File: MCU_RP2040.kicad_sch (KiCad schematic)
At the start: 34 parts, among them X1 ECS-2520MVLC-120-CN

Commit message: Annotation update
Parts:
- renumbered C13 to C7, C15 to C8
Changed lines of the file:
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@@
 			(project "Mad_RP2040"
 				(path "/eedae293-eb5b-47bd-b383-bccfdf81bf72/4e3cb99d-3a42-46ca-abb7-444fcb451820/f42afd4d-da97-4905-9d8b-11c28a037c21"
-					(reference "TP?")
+					(reference "TP2")
 					(unit 1)
 				)
@@
 			(project "Mad_RP2040"
 				(path "/eedae293-eb5b-47bd-b383-bccfdf81bf72/4e3cb99d-3a42-46ca-abb7-444fcb451820/f42afd4d-da97-4905-9d8b-11c28a037c21"
-					(reference "C?")
+					(reference "C14")
 					(unit 1)
 				)
@@
 			(project "Mad_RP2040"
 				(path "/eedae293-eb5b-47bd-b383-bccfdf81bf72/4e3cb99d-3a42-46ca-abb7-444fcb451820/f42afd4d-da97-4905-9d8b-11c28a037c21"
-					(reference "Q?")
+					(reference "Q1")
 					(unit 2)
 				)
@@
 			(project "Mad_RP2040"
 				(path "/eedae293-eb5b-47bd-b383-bccfdf81bf72/4e3cb99d-3a42-46ca-abb7-444fcb451820/f42afd4d-da97-4905-9d8b-11c28a037c21"
-					(reference "R?")
+					(reference "R7")
 					(unit 1)
 				)
@@
 			(project "Mad_RP2040"
 				(path "/eedae293-eb5b-47bd-b383-bccfdf81bf72/4e3cb99d-3a42-46ca-abb7-444fcb451820/f42afd4d-da97-4905-9d8b-11c28a037c21"
-					(reference "U?")
+					(reference "U5")
 					(unit 1)
 				)
@@
 			(project "Mad_RP2040"
 				(path "/eedae293-eb5b-47bd-b383-bccfdf81bf72/4e3cb99d-3a42-46ca-abb7-444fcb451820/f42afd4d-da97-4905-9d8b-11c28a037c21"
-					(reference "R?")
+					(reference "R6")
 					(unit 1)
 				)
@@
 			(project "Mad_RP2040"
 				(path "/eedae293-eb5b-47bd-b383-bccfdf81bf72/4e3cb99d-3a42-46ca-abb7-444fcb451820/f42afd4d-da97-4905-9d8b-11c28a037c21"
-					(reference "C?")
+					(reference "C9")
 					(unit 1)
 				)
@@
 			(project "Mad_RP2040"
 				(path "/eedae293-eb5b-47bd-b383-bccfdf81bf72/4e3cb99d-3a42-46ca-abb7-444fcb451820/f42afd4d-da97-4905-9d8b-11c28a037c21"
-					(reference "C?")
+					(reference "C10")
 					(unit 1)
 				)
@@
 			(project "Mad_RP2040"
 				(path "/eedae293-eb5b-47bd-b383-bccfdf81bf72/4e3cb99d-3a42-46ca-abb7-444fcb451820/f42afd4d-da97-4905-9d8b-11c28a037c21"
-					(reference "C?")
+					(reference "C13")
 					(unit 1)
 				)
@@
 			(project "Mad_RP2040"
 				(path "/eedae293-eb5b-47bd-b383-bccfdf81bf72/4e3cb99d-3a42-46ca-abb7-444fcb451820/f42afd4d-da97-4905-9d8b-11c28a037c21"
-					(reference "C?")
+					(reference "C11")
 					(unit 1)
 				)
@@
 			(project "Mad_RP2040"
 				(path "/eedae293-eb5b-47bd-b383-bccfdf81bf72/4e3cb99d-3a42-46ca-abb7-444fcb451820/f42afd4d-da97-4905-9d8b-11c28a037c21"
-					(reference "U?")
+					(reference "U4")
 					(unit 1)
 				)
@@
 			(project "Mad_RP2040"
 				(path "/eedae293-eb5b-47bd-b383-bccfdf81bf72/4e3cb99d-3a42-46ca-abb7-444fcb451820/f42afd4d-da97-4905-9d8b-11c28a037c21"
-					(reference "TP?")
+					(reference "TP3")
 					(unit 1)
 				)
@@
 			(project "Mad_RP2040"
 				(path "/eedae293-eb5b-47bd-b383-bccfdf81bf72/4e3cb99d-3a42-46ca-abb7-444fcb451820/f42afd4d-da97-4905-9d8b-11c28a037c21"
-					(reference "C?")
+					(reference "C6")
 					(unit 1)
 				)
@@
 			(project "Mad_RP2040"
 				(path "/eedae293-eb5b-47bd-b383-bccfdf81bf72/4e3cb99d-3a42-46ca-abb7-444fcb451820/f42afd4d-da97-4905-9d8b-11c28a037c21"
-					(reference "D?")
+					(reference "D7")
 					(unit 1)
 				)
@@
 			(project "Mad_RP2040"
 				(path "/eedae293-eb5b-47bd-b383-bccfdf81bf72/4e3cb99d-3a42-46ca-abb7-444fcb451820/f42afd4d-da97-4905-9d8b-11c28a037c21"
-					(reference "C?")
+					(reference "C16")
 					(unit 1)
 				)
@@
 			(project "Mad_RP2040"
 				(path "/eedae293-eb5b-47bd-b383-bccfdf81bf72/4e3cb99d-3a42-46ca-abb7-444fcb451820/f42afd4d-da97-4905-9d8b-11c28a037c21"
-					(reference "Q?")
+					(reference "Q1")
 					(unit 1)
 				)
@@
 			(project "Mad_RP2040"
 				(path "/eedae293-eb5b-47bd-b383-bccfdf81bf72/4e3cb99d-3a42-46ca-abb7-444fcb451820/f42afd4d-da97-4905-9d8b-11c28a037c21"
-					(reference "R?")
+					(reference "R9")
 					(unit 1)
 				)
@@
 		(on_board yes)
 		(dnp no)
-		(property "Reference" "C13"
+		(property "Reference" "C7"
 			(at 52.705 73.66 0)
 			(effects
@@
 			(project "Mad_RP2040"
 				(path "/eedae293-eb5b-47bd-b383-bccfdf81bf72/4e3cb99d-3a42-46ca-abb7-444fcb451820/f42afd4d-da97-4905-9d8b-11c28a037c21"
-					(reference "C13")
+					(reference "C7")
 					(unit 1)
 				)
@@
 			(project "Mad_RP2040"
 				(path "/eedae293-eb5b-47bd-b383-bccfdf81bf72/4e3cb99d-3a42-46ca-abb7-444fcb451820/f42afd4d-da97-4905-9d8b-11c28a037c21"
-					(reference "C?")
+					(reference "C17")
 					(unit 1)
 				)
@@
 			(project "Mad_RP2040"
 				(path "/eedae293-eb5b-47bd-b383-bccfdf81bf72/4e3cb99d-3a42-46ca-abb7-444fcb451820/f42afd4d-da97-4905-9d8b-11c28a037c21"
-					(reference "C?")
+					(reference "C12")
 					(unit 1)
 				)
@@
 			(project "Mad_RP2040"
 				(path "/eedae293-eb5b-47bd-b383-bccfdf81bf72/4e3cb99d-3a42-46ca-abb7-444fcb451820/f42afd4d-da97-4905-9d8b-11c28a037c21"
-					(reference "C?")
+					(reference "C15")
 					(unit 1)
 				)
@@
 			(project "Mad_RP2040"
 				(path "/eedae293-eb5b-47bd-b383-bccfdf81bf72/4e3cb99d-3a42-46ca-abb7-444fcb451820/f42afd4d-da97-4905-9d8b-11c28a037c21"
-					(reference "TP?")
+					(reference "TP1")
 					(unit 1)
 				)
@@
 			(project "Mad_RP2040"
 				(path "/eedae293-eb5b-47bd-b383-bccfdf81bf72/4e3cb99d-3a42-46ca-abb7-444fcb451820/f42afd4d-da97-4905-9d8b-11c28a037c21"
-					(reference "R?")
+					(reference "R12")
 					(unit 1)
 				)
@@
 			(project "Mad_RP2040"
 				(path "/eedae293-eb5b-47bd-b383-bccfdf81bf72/4e3cb99d-3a42-46ca-abb7-444fcb451820/f42afd4d-da97-4905-9d8b-11c28a037c21"
-					(reference "R?")
+					(reference "R8")
 					(unit 1)
 				)
@@
 			(project "Mad_RP2040"
 				(path "/eedae293-eb5b-47bd-b383-bccfdf81bf72/4e3cb99d-3a42-46ca-abb7-444fcb451820/f42afd4d-da97-4905-9d8b-11c28a037c21"
-					(reference "R?")
+					(reference "R13")
 					(unit 1)
 				)
@@
 			(project "Mad_RP2040"
 				(path "/eedae293-eb5b-47bd-b383-bccfdf81bf72/4e3cb99d-3a42-46ca-abb7-444fcb451820/f42afd4d-da97-4905-9d8b-11c28a037c21"
-					(reference "R?")
+					(reference "R14")
 					(unit 1)
 				)
@@
 			(project "Mad_RP2040"
 				(path "/eedae293-eb5b-47bd-b383-bccfdf81bf72/4e3cb99d-3a42-46ca-abb7-444fcb451820/f42afd4d-da97-4905-9d8b-11c28a037c21"
-					(reference "SW?")
+					(reference "SW3")
 					(unit 1)
 				)
@@
 			(project "Mad_RP2040"
 				(path "/eedae293-eb5b-47bd-b383-bccfdf81bf72/4e3cb99d-3a42-46ca-abb7-444fcb451820/f42afd4d-da97-4905-9d8b-11c28a037c21"
-					(reference "C?")
+					(reference "C20")
 					(unit 1)
 				)
@@
 			(project "Mad_RP2040"
 				(path "/eedae293-eb5b-47bd-b383-bccfdf81bf72/4e3cb99d-3a42-46ca-abb7-444fcb451820/f42afd4d-da97-4905-9d8b-11c28a037c21"
-					(reference "R?")
+					(reference "R11")
 					(unit 1)
 				)
@@
 			(project "Mad_RP2040"
 				(path "/eedae293-eb5b-47bd-b383-bccfdf81bf72/4e3cb99d-3a42-46ca-abb7-444fcb451820/f42afd4d-da97-4905-9d8b-11c28a037c21"
-					(reference "C?")
+					(reference "C18")
 					(unit 1)
 				)
@@
 			(project "Mad_RP2040"
 				(path "/eedae293-eb5b-47bd-b383-bccfdf81bf72/4e3cb99d-3a42-46ca-abb7-444fcb451820/f42afd4d-da97-4905-9d8b-11c28a037c21"
-					(reference "C?")
+					(reference "C19")
 					(unit 1)
 				)
@@
 		(dnp yes)
 		(fields_autoplaced yes)
-		(property "Reference" "C15"
+		(property "Reference" "C8"
 			(at 86.36 180.3462 0)
 			(effects
@@
 			(project "Mad_RP2040"
 				(path "/eedae293-eb5b-47bd-b383-bccfdf81bf72/4e3cb99d-3a42-46ca-abb7-444fcb451820/f42afd4d-da97-4905-9d8b-11c28a037c21"
-					(reference "C15")
+					(reference "C8")
 					(unit 1)
 				)

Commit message: Board update
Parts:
- removed C? (x2): 100nF, Capacitor_SMD:C_0402_1005Metric, symbol Device:C_Small
- added C19, C20, C21: 100nF, Capacitor_SMD:C_0402_1005Metric, symbol Device:C_Small
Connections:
- net 1V1: now also C20.1, C21.1
- net 3V3: now also C19.1
- net GND: now also C19.2, C20.2, C21.2
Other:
- moved on the sheet: C?

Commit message: Cleanup bom, remove spaces and lcsc fields
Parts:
- D?: Price $0.21 -> $0.21
- Q? (x2): Price $0.64 -> $0.64
- R10, R? (x8): Price $0.16 -> $0.16
- SW?: Price $0.41 -> $0.41
- U?: Price $1.11 -> $1.11
- U?: Price $3.48 -> $3.48

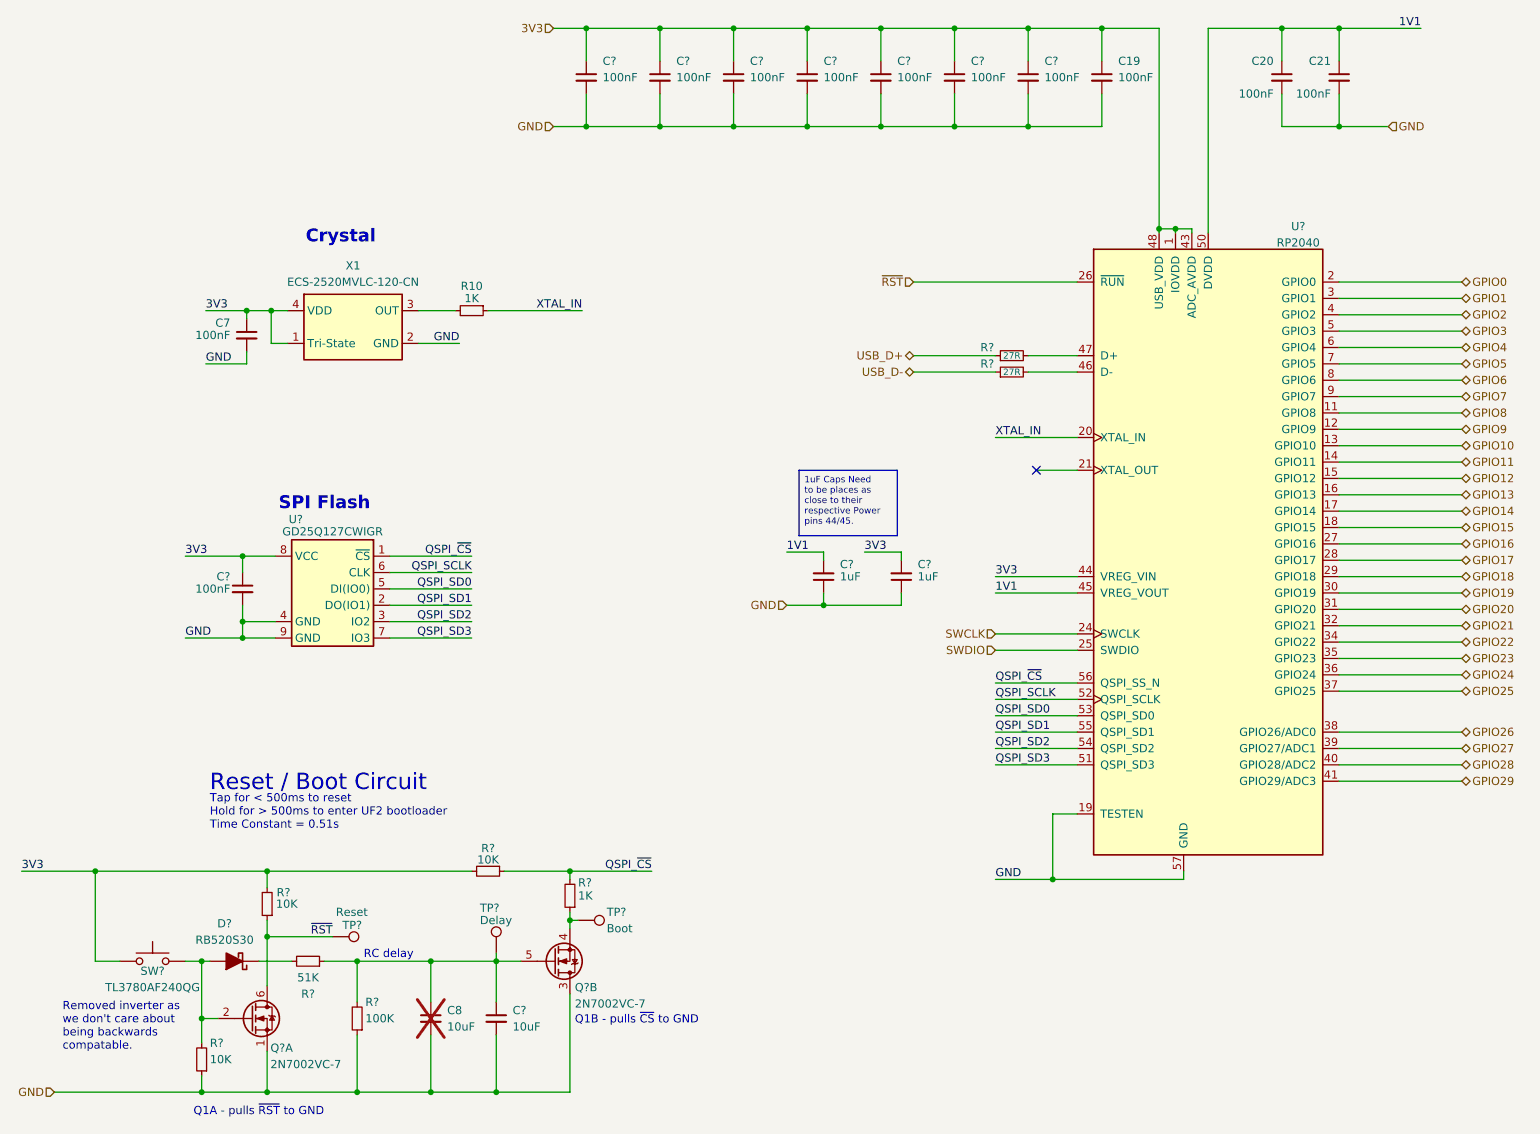
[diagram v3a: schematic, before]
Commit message: Update Models, Finalize LED selections, add backlight, ...
 add mounting holes, add fids, cleanup
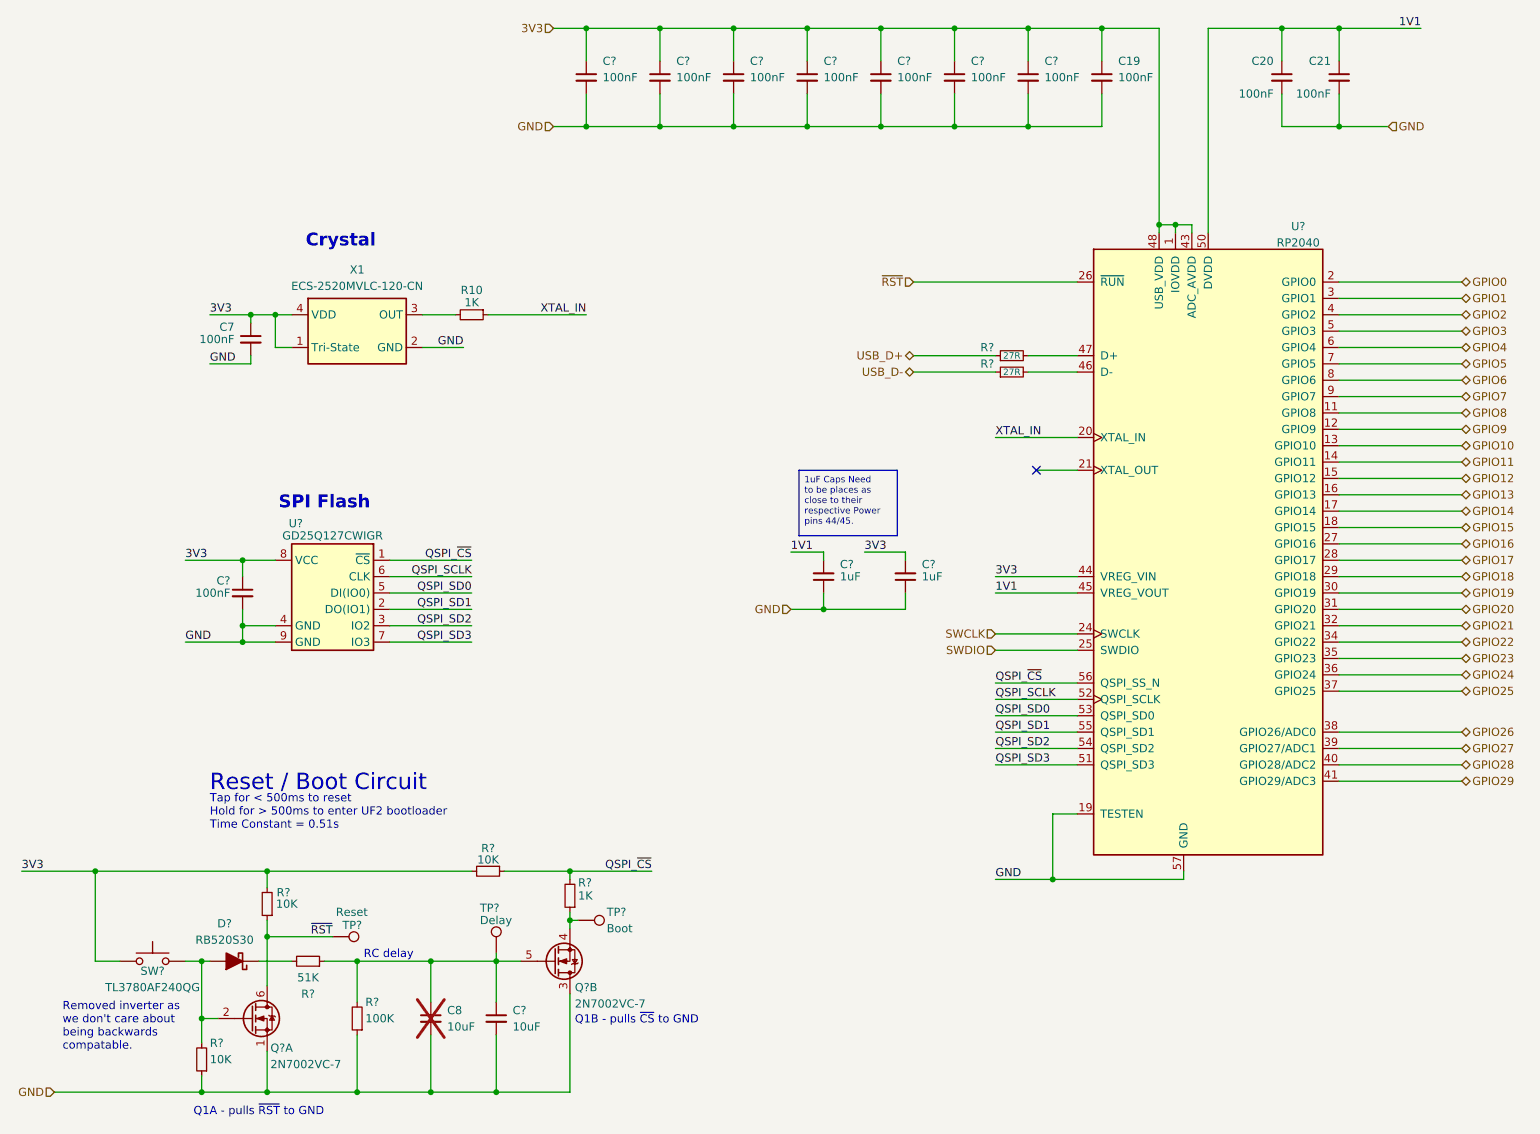
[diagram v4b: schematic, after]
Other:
- company: MadMan -> ${COMPANY}
- title: RP2040 -> ${TITLE}
- moved on the sheet: C7, C?, R10, U?, X1

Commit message: BOM update, add lcsc pn to  componenets.
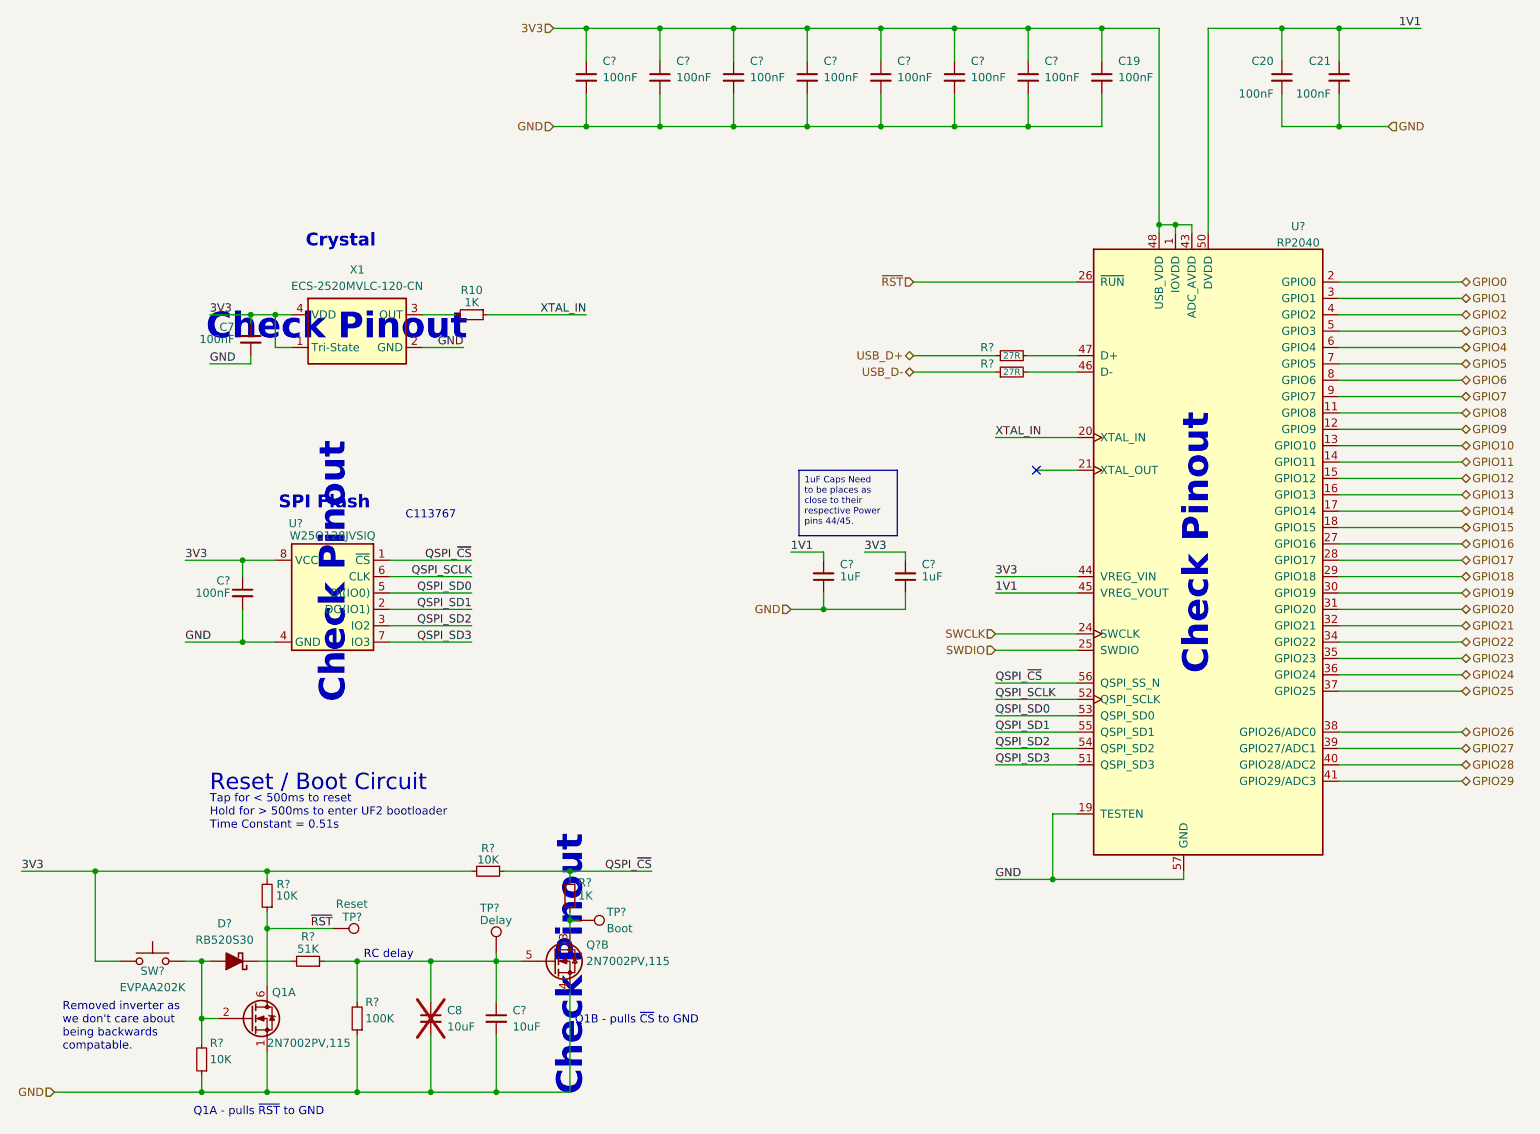
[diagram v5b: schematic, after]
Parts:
- removed Q?: 2N7002VC-7, Package_TO_SOT_SMD:SOT-363_SC-70-6, symbol Transistor_FET:FDG6335N
- added Q1: 2N7002PV,115, Package_TO_SOT_SMD:SOT-666, symbol Transistor_FET:FDG6335N
- C? (x2): LCSC PN (none) -> C14664
- D?: LCSC PN (none) -> C232575
- Q?: value 2N7002VC-7 -> 2N7002PV,115; footprint Package_TO_SOT_SMD:SOT-363_SC-70-6 -> Package_TO_SOT_SMD:SOT-666; LCSC PN (none) -> C551422; MPN 2N7002VC-7 -> 2N7002PV,115; Rating MOSFET 2N-CH 60V 0.28A SOT563 -> MOSFET 2N-CH 60V 0.35A SOT666; Supplier PN 2N7002VC-7DICT-ND -> 1727-4792-1-ND
- R10, R?: LCSC PN (none) -> C106235
- R? (x3): LCSC PN (none) -> C60490
- R?: LCSC PN (none) -> C60491
- R?: LCSC PN (none) -> C107229
- R? (x2): LCSC PN (none) -> C138021
- SW?: value TL3780AF240QG -> EVPAA202K; footprint Mad_Footprints:SW_TL3780AF240QG -> Mad_Footprints:EVP-AA202K; MPN TL3780AF240QG -> EVPAA202K; Manufacturer E-Switch -> Panasonic Electronic Components; Price $0.41 -> $1.26; Rating SWITCH TACTILE SPST-NO 0.05A 12V -> SWITCH TACTILE SPST-NO 0.02A 15V; Supplier PN EG5393CT-ND -> P13348SCT-ND
- U?: LCSC PN (none) -> C2040
- U?: value GD25Q127CWIGR -> W25Q128JVSIQ; footprint Mad_Footprints:GD25LQ128DYIGR -> Package_SO:SOIC-8_5.23x5.23mm_P1.27mm; LCSC PN (none) -> C97521; MPN GD25Q127CWIGR -> W25Q128JVSIQ; Manufacturer GigaDevice Semiconductor (HK) Limited -> Winbond Electronics; Price $3.48 -> $2.72; Rating IC FLASH 128MBIT SPI/QUAD 8WSON -> IC FLASH 128MBIT SPI/QUAD 8SOIC; Supplier PN 1970-1048-1-ND -> W25Q128JVSIQ-ND
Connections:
- net 3V3: now also SW?.1; no longer SW?.2
- net GND: now also Q?.4 (S), Q1.1 (S); no longer Q?.3 (D), U?.9 (GND)
- net ~{RST}: now also Q1.6 (D)
- net at R?.1, TP?.1: now also Q?.3 (D); no longer Q?.4 (S)
- net at D?.2 (A), R?.2: now also SW?.2, Q1.2 (G); no longer SW?.1
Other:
- note added: "C113767"
- note added: "Check Pinout"
- moved on the sheet: R?, TP?
